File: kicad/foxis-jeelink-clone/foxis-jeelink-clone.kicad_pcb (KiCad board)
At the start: 2 copper layers, 19.5 x 50.2 mm, 27 parts, among them J1 USB_A, J2 AVR-ISP-6, J3 SMA connector, J4 WireAntenna, U1 ATmega328P-A, U2 FT232RL, U3 RFM69CW, X1 16 MHz

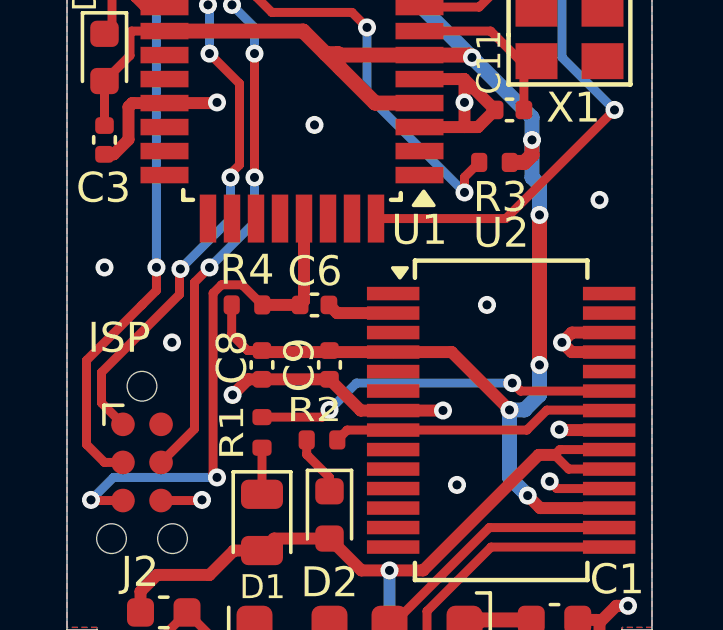
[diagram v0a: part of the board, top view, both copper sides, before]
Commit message: fix massive error that made Rev. 0 completely nonfunctional. I simply forgot to connect RX and TX. Absolutely no idea how I managed to mess this up.
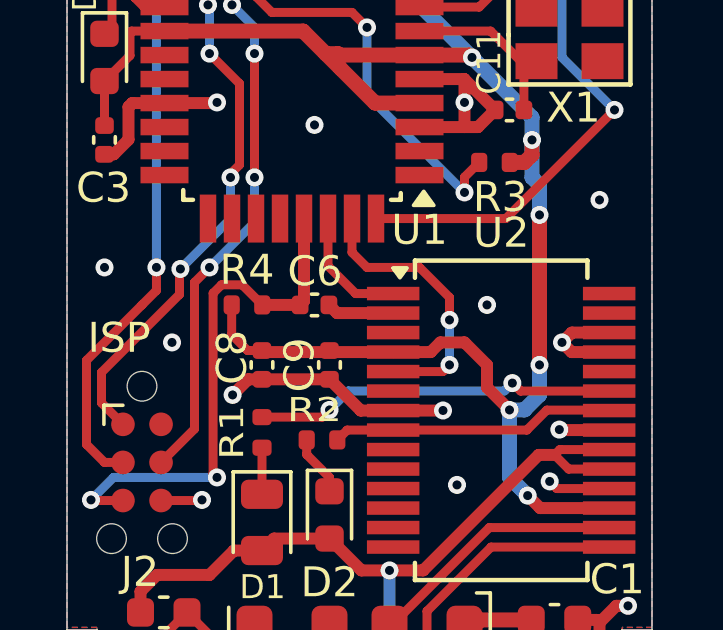
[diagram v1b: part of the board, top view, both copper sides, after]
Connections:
- U1 pad 30: unconnected-(U1-PD0-Pad30) -> /MC-RX
- U1 pad 31: unconnected-(U1-PD1-Pad31) -> /MC-TX
- U2 pad 1: unconnected-(U2-TXD-Pad1) -> /MC-RX
- U2 pad 5: unconnected-(U2-RXD-Pad5) -> /MC-TX
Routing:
- net /MC-TX: track 0.00 -> 9.22 mm, vias 0 -> 2
- net /MC-RX: track 0.00 -> 4.13 mm
- net +3V3: track 91.0 -> 91.7 mm
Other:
- board text added: "Rev. 1"

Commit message: rev. 1 as sent to JLCPCB
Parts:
- added C12: 22uF, Capacitor_SMD:C_0603_1608Metric, F.Cu at (117.5, 129.8)
- moved J4 2.00 mm to (104.5, 102.0)
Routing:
- net GND: track 63.6 -> 69.8 mm
- net +3V3: track 91.7 -> 92.7 mm
- net Net-(J3-In): track 17.4 -> 16.5 mm
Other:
- outline, holes or cut-outs redrawn
- board text added: "3V3"
- board text added: "GND"
- board text added: "www.poempelfox.de/jeelink-clone"
